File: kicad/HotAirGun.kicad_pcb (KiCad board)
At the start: 2 copper layers, 176 x 82.5 mm, 77 parts, among them J1 CONN_02X03, J10 CONN_01X06, J2 CONN_01X06, J3 CONN_02X02, J4 HAG Resistor, J5 PWR_IN, J6 PWR_Suply, J7 Vin, J8 Foot Switch, J9 CONN_01X06, Q1 Q_NPN_CBE, Q2 Q_PNP_CBE, Q3 IRF740, SW1 Start, SW2 Stop, SW3 WeldCurv, SW4 Rotary_Encoder_Switch_V2, U1 MCP23017, U2 MOC3023M, U3 LM2575, U4 MAX6675

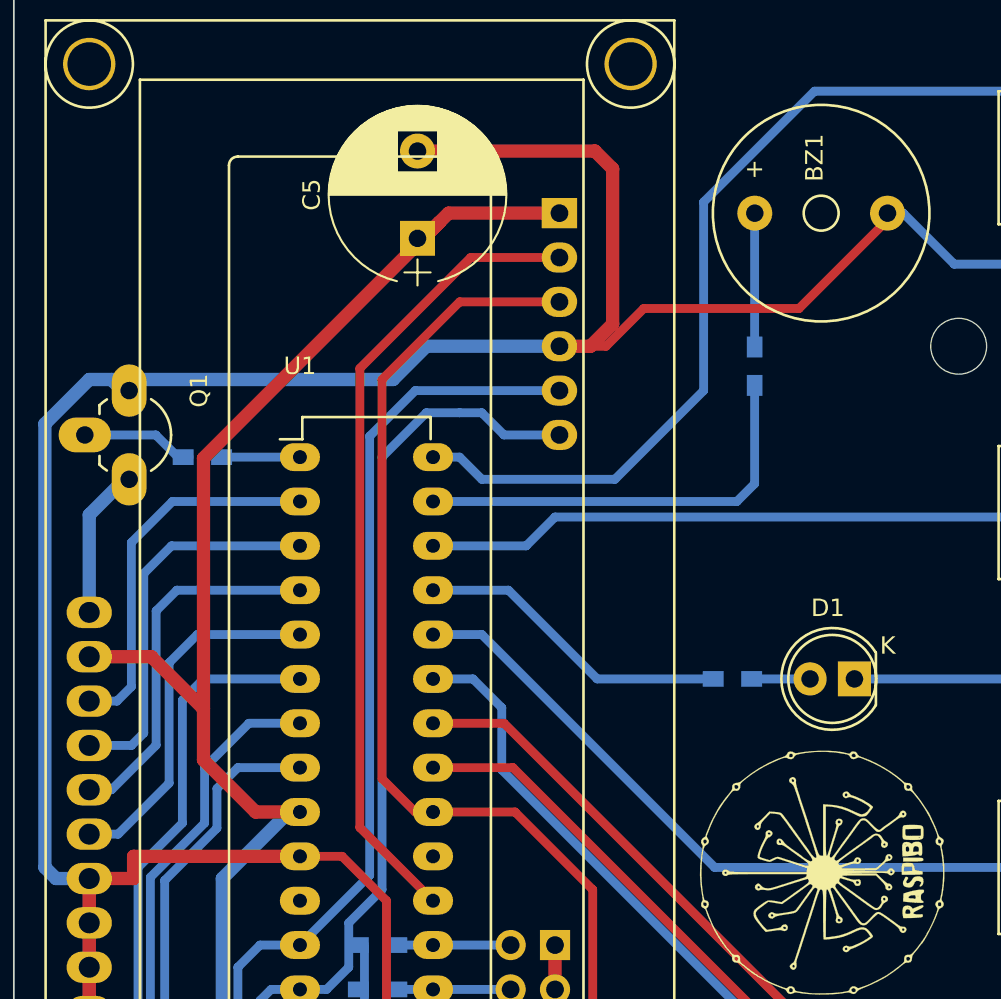
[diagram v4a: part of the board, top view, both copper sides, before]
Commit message: Added C6 bypass capacitor
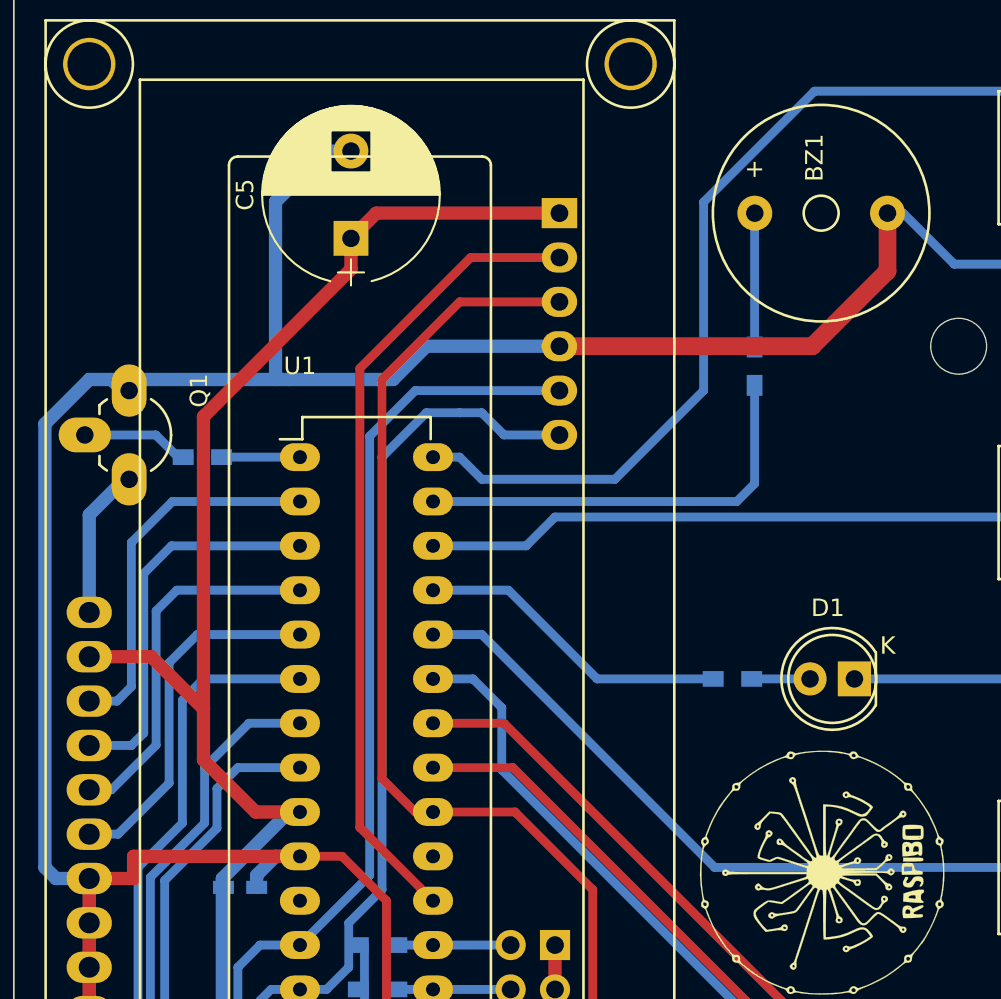
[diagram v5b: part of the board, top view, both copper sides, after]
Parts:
- added C6: 100nf, Capacitors_SMD:C_0603_HandSoldering, B.Cu at (176.3, 107.4)
- C3: value C -> 100nF
- moved C5 3.81 mm to (182.6, 70.3)
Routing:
- net Gnd_P: track 329.9 -> 329.1 mm
- net Vcc_P: track 158.9 -> 159.6 mm
